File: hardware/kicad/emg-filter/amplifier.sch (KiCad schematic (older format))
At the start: 0 parts

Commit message: Non-inverting amplifier (amplifier) implemented.
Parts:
- added R1, R2: 2k, symbol Device:R
- added R3, R4: 10k, symbol Device:R
- added U1: LM4565, symbol emg-filter:LM4565
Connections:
- new net: R1.1, R3.2, U1.2 (-IN1)
- new net: R2.1, R4.2, U1.6 (-IN2)
- new net +5V: U1.8 (VCC)
- new net -5V: U1.4 (VEE)
- new net GND: R1.2, R2.2
- new net INPUT_1_AMPLIFIER: U1.3 (+IN1)
- new net INPUT_2_AMPLIFIER: U1.5 (+IN2)
- new net OUTPUT_1_AMPLFIER: R3.1, U1.1 (OUT1)
- new net OUTPUT_2_AMPLIFIER: R4.1, U1.7 (OUT2)
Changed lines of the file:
@@
 $Descr A4 11693 8268
 encoding utf-8
-Sheet 1 9
+Sheet 7 9
 Title ""
 Date ""
@@
 Comment4 ""
 $EndDescr
+$Comp
+L emg-filter:LM4565 U1
+U 1 1 61C3E8D4
+P 5600 3650
+F 0 "U1" H 5800 4100 50  0000 C CNN
+F 1 "LM4565" H 5900 4000 50  0000 C CNN
+F 2 "" H 6600 3650 50  0001 C CNN
+F 3 "" H 6600 3650 50  0001 C CNN
+	1    5600 3650
+	1    0    0    -1
+$EndComp
+Text GLabel 5100 3750 0    50   Input ~ 0
+INPUT_2_AMPLIFIER
+$Comp
+L Device:R R3
+U 1 1 61C410A1
+P 5600 2850
+F 0 "R3" V 5393 2850 50  0000 C CNN
+F 1 "10k" V 5484 2850 50  0000 C CNN
+F 2 "" V 5530 2850 50  0001 C CNN
+F 3 "~" H 5600 2850 50  0001 C CNN
+	1    5600 2850
+	0    1    1    0
+$EndComp
+Wire Wire Line
+	6100 4500 6100 3850
+Wire Wire Line
+	6100 3850 6000 3850
+Wire Wire Line
+	6100 2850 6100 3500
+Wire Wire Line
+	6100 3500 6000 3500
+$Comp
+L Device:R R2
+U 1 1 61C42A00
+P 4950 4050
+F 0 "R2" H 5020 4096 50  0000 L CNN
+F 1 "2k" H 5020 4005 50  0000 L CNN
+F 2 "" V 4880 4050 50  0001 C CNN
+F 3 "~" H 4950 4050 50  0001 C CNN
+	1    4950 4050
+	1    0    0    -1
+$EndComp
+$Comp
+L power:GND #PWR05
+U 1 1 61C456E8
+P 4950 4250
+F 0 "#PWR05" H 4950 4000 50  0001 C CNN
+F 1 "GND" H 4950 4100 50  0000 C CNN
+F 2 "" H 4950 4250 50  0001 C CNN
+F 3 "" H 4950 4250 50  0001 C CNN
+	1    4950 4250
+	1    0    0    -1
+$EndComp
+Wire Wire Line
+	4950 4200 4950 4250
+Wire Wire Line
+	5150 3850 5200 3850
+Wire Wire Line
+	5200 3600 5150 3600
+Wire Wire Line
+	5150 3850 5150 4500
+Text GLabel 6200 3850 2    50   Input ~ 0
+OUTPUT_2_AMPLIFIER
+Wire Wire Line
+	6200 3850 6100 3850
+Connection ~ 6100 3850
+Text GLabel 6200 3500 2    50   Input ~ 0
+OUTPUT_1_AMPLFIER
+Wire Wire Line
+	6100 3500 6200 3500
+Connection ~ 6100 3500
+Wire Wire Line
+	5150 3600 5150 2850
+Wire Wire Line
+	5150 3850 4950 3850
+Connection ~ 5150 3850
+$Comp
+L power:+5V #PWR06
+U 1 1 61C53EC1
+P 5600 3300
+F 0 "#PWR06" H 5600 3150 50  0001 C CNN
+F 1 "+5V" H 5615 3473 50  0000 C CNN
+F 2 "" H 5600 3300 50  0001 C CNN
+F 3 "" H 5600 3300 50  0001 C CNN
+	1    5600 3300
+	1    0    0    -1
+$EndComp
+Wire Wire Line
+	5150 4500 5450 4500
+Wire Wire Line
+	5750 4500 6100 4500
+$Comp
+L power:-5V #PWR07
+U 1 1 61C5483A
+P 5600 4050
+F 0 "#PWR07" H 5600 4150 50  0001 C CNN
+F 1 "-5V" H 5615 4223 50  0000 C CNN
+F 2 "" H 5600 4050 50  0001 C CNN
+F 3 "" H 5600 4050 50  0001 C CNN
+	1    5600 4050
+	-1   0    0    1
+$EndComp
+$Comp
+L Device:R R4
+U 1 1 61C41765
+P 5600 4500
+F 0 "R4" V 5700 4500 50  0000 C CNN
+F 1 "10k" V 5800 4500 50  0000 C CNN
+F 2 "" V 5530 4500 50  0001 C CNN
+F 3 "~" H 5600 4500 50  0001 C CNN
+	1    5600 4500
+	0    1    1    0
+$EndComp
+Wire Wire Line
+	6100 2850 5750 2850
+Wire Wire Line
+	5450 2850 5150 2850
+Connection ~ 5150 2850
+Wire Wire Line
+	5150 2850 4950 2850
+Wire Wire Line
+	4950 2850 4950 2900
+Text GLabel 5100 3500 0    50   Input ~ 0
+INPUT_1_AMPLIFIER
+Wire Wire Line
+	4950 3200 4950 3250
+$Comp
+L Device:R R1
+U 1 1 61C431CE
+P 4950 3050
+F 0 "R1" H 5020 3096 50  0000 L CNN
+F 1 "2k" H 5020 3005 50  0000 L CNN
+F 2 "" V 4880 3050 50  0001 C CNN
+F 3 "~" H 4950 3050 50  0001 C CNN
+	1    4950 3050
+	1    0    0    -1
+$EndComp
+$Comp
+L power:GND #PWR04
+U 1 1 61C4485E
+P 4950 3250
+F 0 "#PWR04" H 4950 3000 50  0001 C CNN
+F 1 "GND" H 4950 3100 50  0000 C CNN
+F 2 "" H 4950 3250 50  0001 C CNN
+F 3 "" H 4950 3250 50  0001 C CNN
+	1    4950 3250
+	1    0    0    -1
+$EndComp
+Wire Wire Line
+	4950 3850 4950 3900
+Wire Wire Line
+	5200 3500 5100 3500
+Wire Wire Line
+	5200 3750 5100 3750
 $EndSCHEMATC

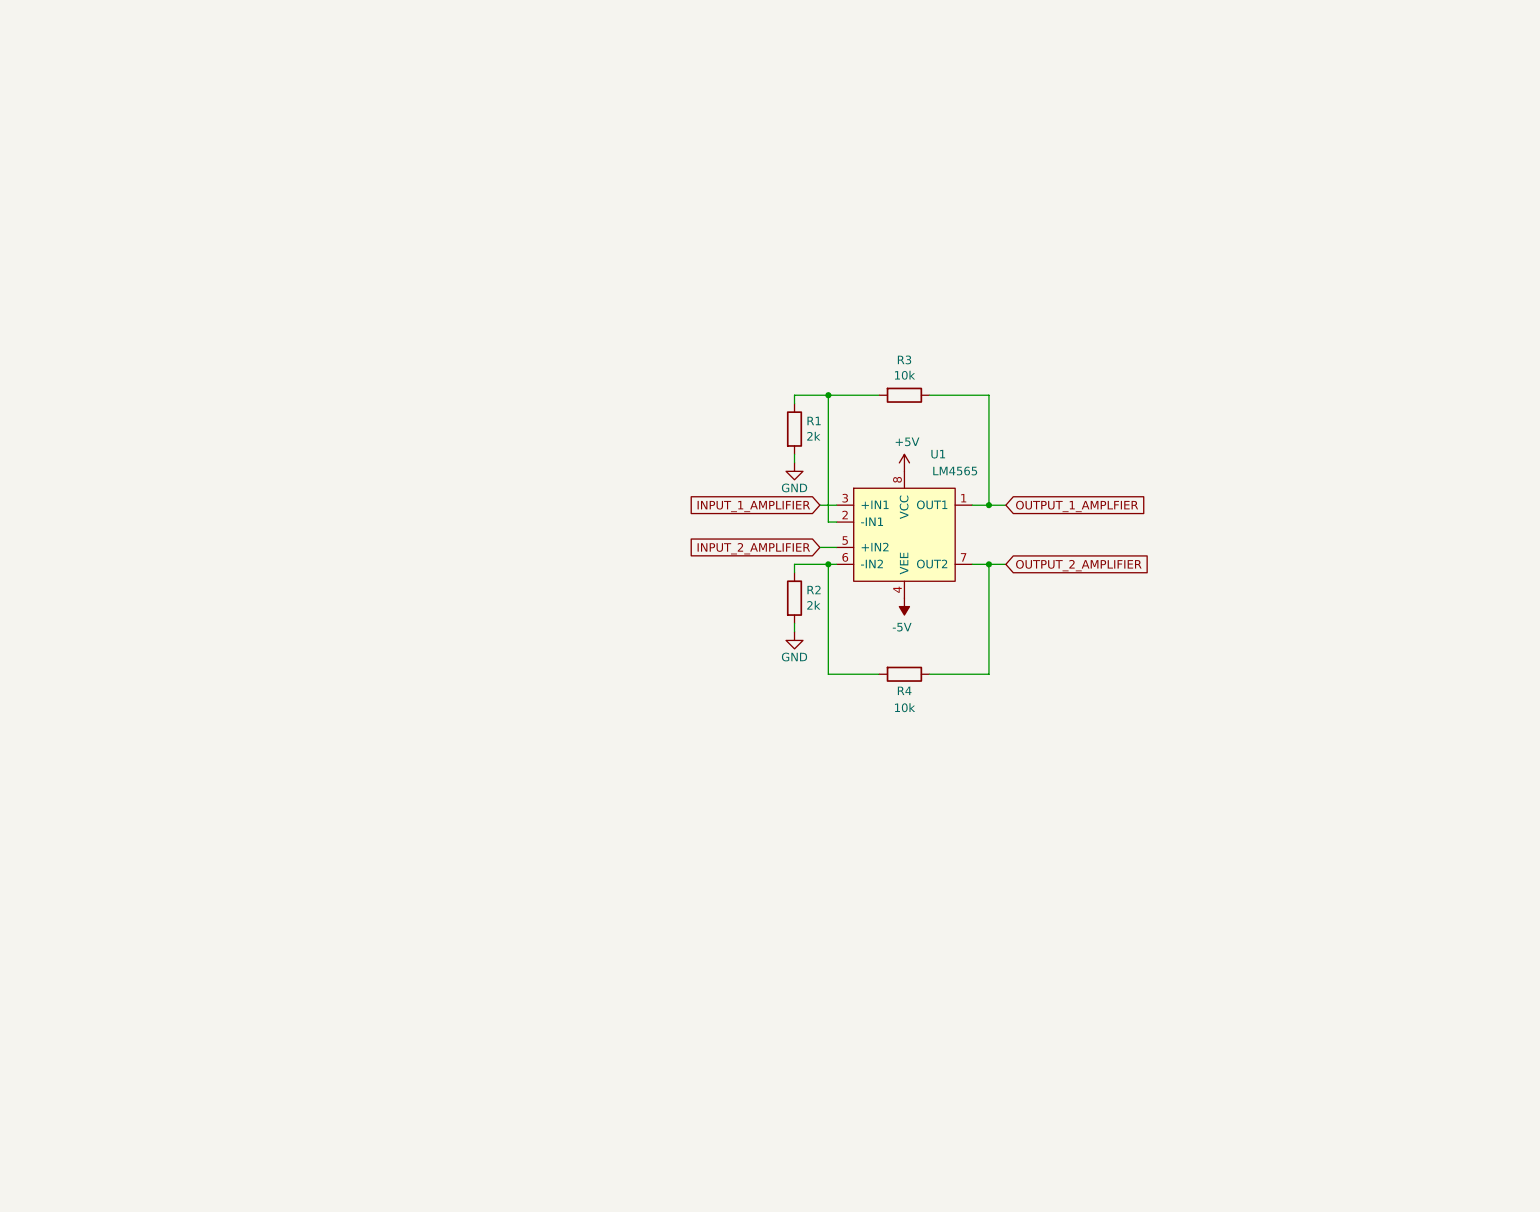
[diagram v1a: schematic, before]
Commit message: 16 non-inverting amplifiers
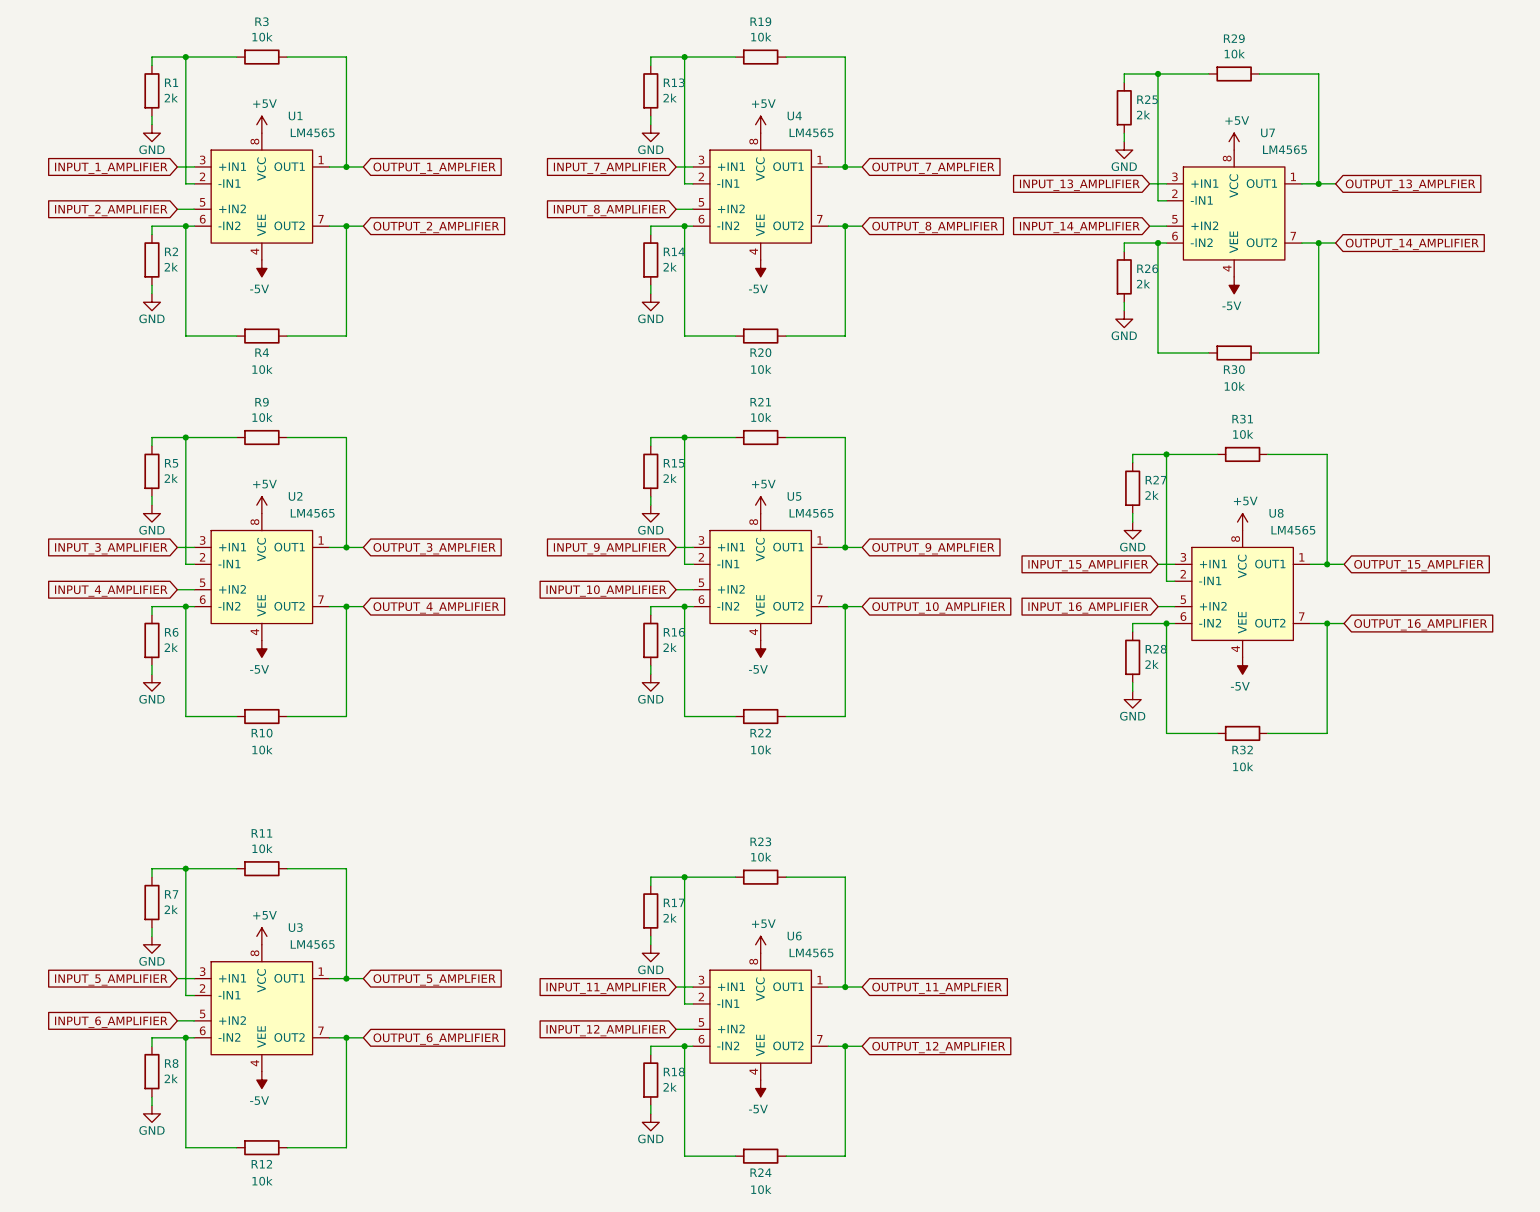
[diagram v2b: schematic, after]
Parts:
- added R10, R11, R12, R19, R20, R21, R22, R23, R24, R29, R30, R31, R32, R9: 10k, symbol Device:R
- added R13, R14, R15, R16, R17, R18, R25, R26, R27, R28, R5, R6, R7, R8: 2k, symbol Device:R
- added U2, U3, U4, U5, U6, U7, U8: LM4565, symbol emg-filter:LM4565
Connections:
- net +5V: now also U2.8 (VCC), U3.8 (VCC), U4.8 (VCC), U5.8 (VCC), U6.8 (VCC), U7.8 (VCC), U8.8 (VCC)
- net -5V: now also U2.4 (VEE), U3.4 (VEE), U4.4 (VEE), U5.4 (VEE), U6.4 (VEE), U7.4 (VEE), U8.4 (VEE)
- net GND: now also R13.2, R14.2, R15.2, R16.2, R17.2, R18.2, R25.2, R26.2, R27.2, R28.2, R5.2, R6.2, R7.2, R8.2
- new net: R5.1, R9.2, U2.2 (-IN1)
- new net: R10.2, R6.1, U2.6 (-IN2)
- new net: R13.1, R19.2, U4.2 (-IN1)
- new net: R14.1, R20.2, U4.6 (-IN2)
- new net: R15.1, R21.2, U5.2 (-IN1)
- new net: R16.1, R22.2, U5.6 (-IN2)
- new net: R25.1, R29.2, U7.2 (-IN1)
- new net: R26.1, R30.2, U7.6 (-IN2)
- new net: R27.1, R31.2, U8.2 (-IN1)
- new net: R28.1, R32.2, U8.6 (-IN2)
- new net: R11.2, R7.1, U3.2 (-IN1)
- new net: R12.2, R8.1, U3.6 (-IN2)
- new net: R17.1, R23.2, U6.2 (-IN1)
- new net: R18.1, R24.2, U6.6 (-IN2)
- new net INPUT_10_AMPLIFIER: U5.5 (+IN2)
- new net INPUT_11_AMPLIFIER: U6.3 (+IN1)
- new net INPUT_12_AMPLIFIER: U6.5 (+IN2)
- new net INPUT_13_AMPLIFIER: U7.3 (+IN1)
- new net INPUT_14_AMPLIFIER: U7.5 (+IN2)
- new net INPUT_15_AMPLIFIER: U8.3 (+IN1)
- new net INPUT_16_AMPLIFIER: U8.5 (+IN2)
- new net INPUT_3_AMPLIFIER: U2.3 (+IN1)
- new net INPUT_4_AMPLIFIER: U2.5 (+IN2)
- new net INPUT_5_AMPLIFIER: U3.3 (+IN1)
- new net INPUT_6_AMPLIFIER: U3.5 (+IN2)
- new net INPUT_7_AMPLIFIER: U4.3 (+IN1)
- new net INPUT_8_AMPLIFIER: U4.5 (+IN2)
- new net INPUT_9_AMPLIFIER: U5.3 (+IN1)
- new net OUTPUT_10_AMPLIFIER: R22.1, U5.7 (OUT2)
- new net OUTPUT_11_AMPLFIER: R23.1, U6.1 (OUT1)
- new net OUTPUT_12_AMPLIFIER: R24.1, U6.7 (OUT2)
- new net OUTPUT_13_AMPLFIER: R29.1, U7.1 (OUT1)
- new net OUTPUT_14_AMPLIFIER: R30.1, U7.7 (OUT2)
- new net OUTPUT_15_AMPLFIER: R31.1, U8.1 (OUT1)
- new net OUTPUT_16_AMPLIFIER: R32.1, U8.7 (OUT2)
- new net OUTPUT_3_AMPLFIER: R9.1, U2.1 (OUT1)
- new net OUTPUT_4_AMPLIFIER: R10.1, U2.7 (OUT2)
- new net OUTPUT_5_AMPLFIER: R11.1, U3.1 (OUT1)
- new net OUTPUT_6_AMPLIFIER: R12.1, U3.7 (OUT2)
- new net OUTPUT_7_AMPLFIER: R19.1, U4.1 (OUT1)
- new net OUTPUT_8_AMPLIFIER: R20.1, U4.7 (OUT2)
- new net OUTPUT_9_AMPLFIER: R21.1, U5.1 (OUT1)
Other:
- moved on the sheet: R1, R2, R3, R4, U1
